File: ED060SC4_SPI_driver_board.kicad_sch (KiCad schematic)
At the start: 27 parts, among them J2 Conn_01x06, J3 Conn_01x04, J4 Conn_01x04, SW1 SS12D07VG2, SW2 DSIC01LSGET, U2 STM32F103C8T6, U3 USBLC6-4SC6, U4 USBLC6-2SC6, U5 USBLC6-2SC6, Y1 16MHz, 10pF

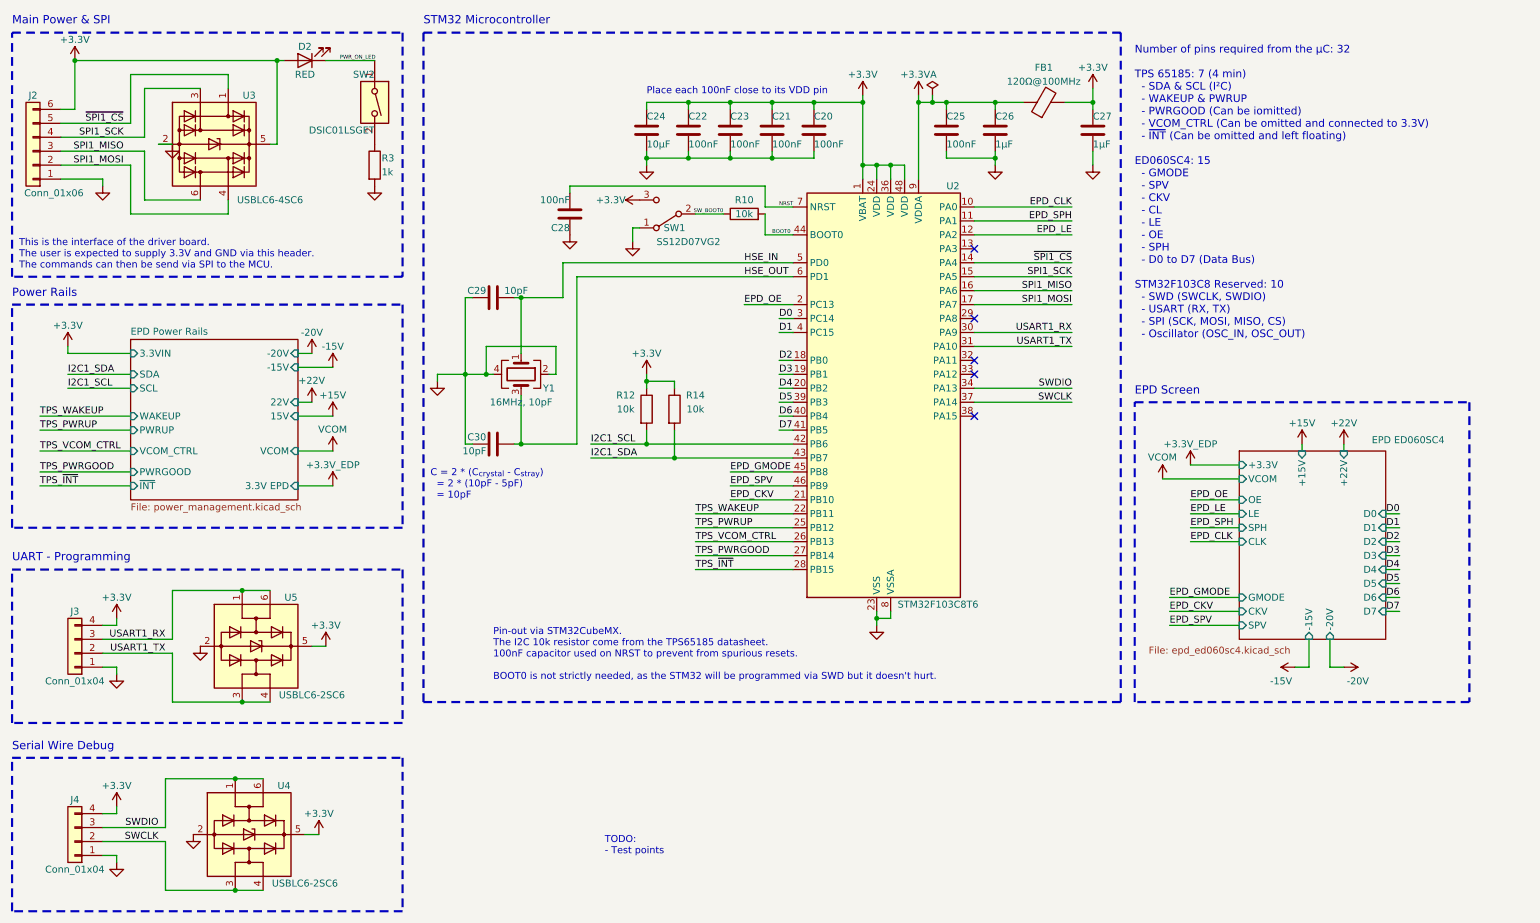
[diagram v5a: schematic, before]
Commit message: Fixed PWR flags in schematic
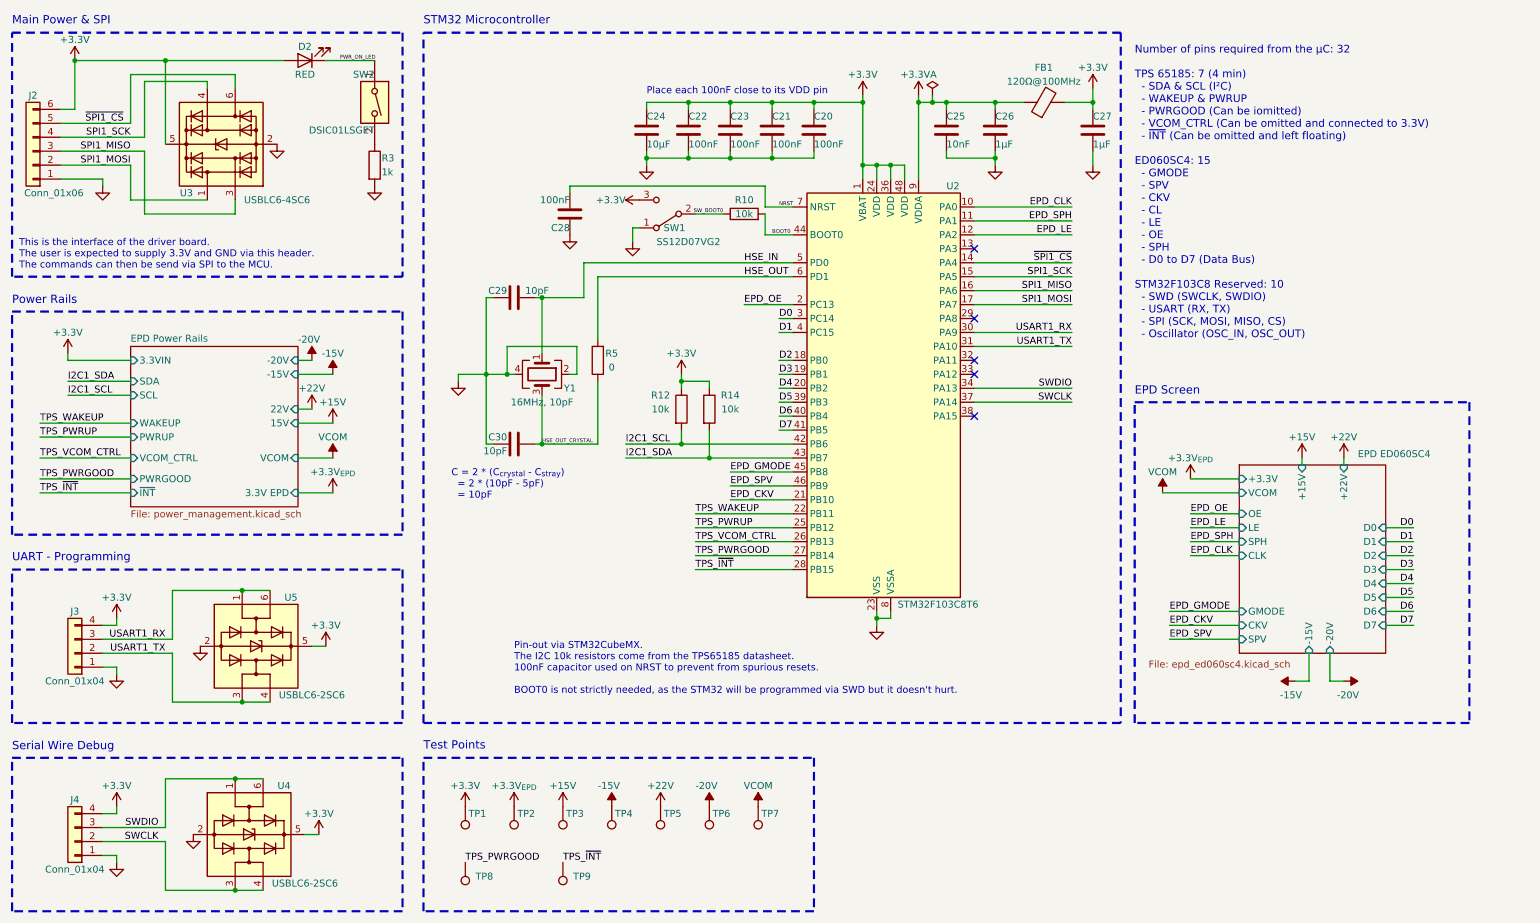
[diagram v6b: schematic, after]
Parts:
- added R5: 0, Resistor_SMD:R_0603_1608Metric, symbol Device:R
- added TP1, TP2, TP3, TP4, TP5, TP6, TP7, TP8, TP9: TestPoint, TestPoint:TestPoint_Pad_D1.0mm, symbol Connector:TestPoint
- C25: value 100nF -> 10nF
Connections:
- net +3.3V: now also TP1.1
- net HSE_OUT: now also R5.2; no longer C30.2, Y1.3
- net SPI1_MISO: now also U3.3 (I/O2); no longer U3.6 (I/O4)
- net SPI1_MOSI: now also U3.1 (I/O1); no longer U3.4 (I/O3)
- net SPI1_SCK: now also U3.4 (I/O3); no longer U3.3 (I/O2)
- net TPS_PWRGOOD: now also TP8.1
- net TPS_~{INT}: now also TP9.1
- net ~{SPI1_CS}: now also U3.6 (I/O4); no longer U3.1 (I/O1)
- new net +15V: TP3.1
- new net +22V: TP5.1
- new net +3.3V_{EPD}: TP2.1
- new net -15V: TP4.1
- new net -20V: TP6.1
- new net HSE_OUT_CRYSTAL: C30.2, R5.1, Y1.3
- new net VCOM: TP7.1
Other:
- note added: "Pin-out via STM32CubeMX. The I2C 10k resistors come from the TPS65185 datasheet. 100nF capacitor used on NRST to prevent from spurious resets. BOOT0 is not strictly needed, as the STM32 will be programmed via SWD but it doesn't hurt."
- note added: "Test Points"
- note removed: "Pin-out via STM32CubeMX. The I2C 10k resistor come from the TPS65185 datasheet. 100nF capacitor used on NRST to prevent from spurious resets. BOOT0 is not strictly needed, as the STM32 will be programmed via SWD but it doesn't hurt."
- note removed: "TODO: - Test points"
- moved on the sheet: C29, C30, R12, R14, U3, Y1

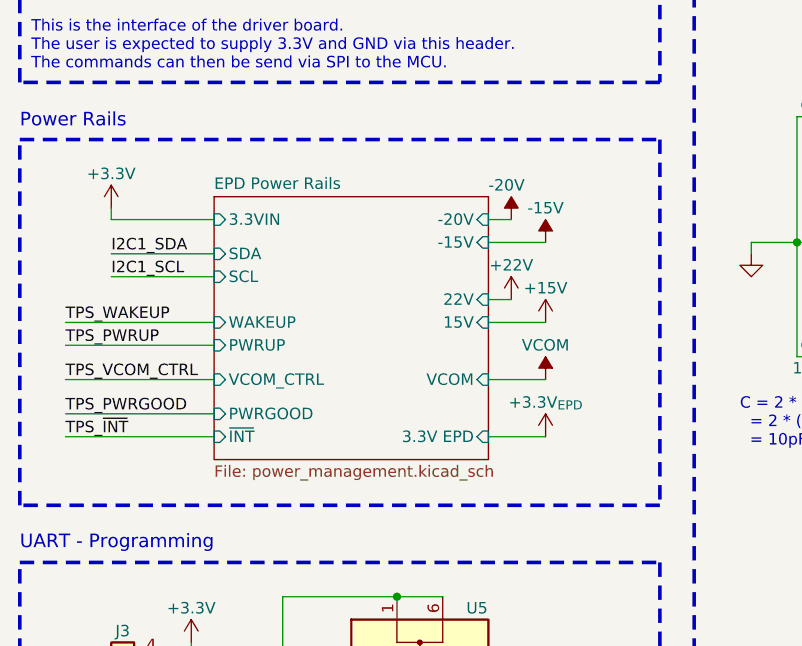
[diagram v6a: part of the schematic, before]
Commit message: Add a connector for easy access to voltages
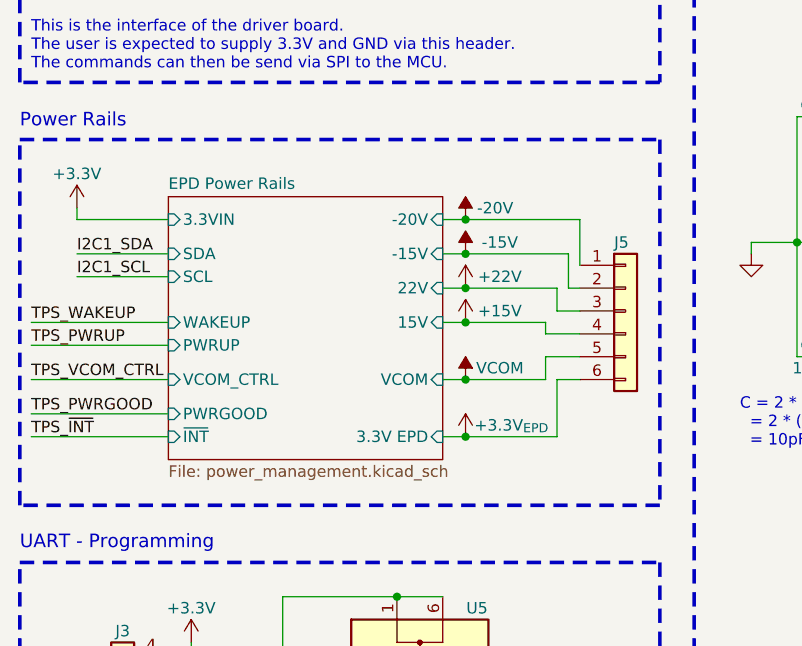
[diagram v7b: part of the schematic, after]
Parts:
- added J5: Conn_01x06, Connector_PinSocket_2.54mm:PinSocket_1x06_P2.54mm_Vertical, symbol Connector_Generic:Conn_01x06
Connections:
- net +15V: now also J5.4 (Pin_4)
- net +22V: now also J5.3 (Pin_3)
- net +3.3V_{EPD}: now also J5.6 (Pin_6)
- net -15V: now also J5.2 (Pin_2)
- net -20V: now also J5.1 (Pin_1)
- net VCOM: now also J5.5 (Pin_5)

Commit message: PCB routing
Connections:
- net SPI1_MISO: now also U3.1 (I/O1); no longer U3.3 (I/O2)
- net SPI1_MOSI: now also U3.3 (I/O2); no longer U3.1 (I/O1)
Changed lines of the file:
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@@
-    (stroke (width 0) (type default))
-  )
-  (wire (pts (xy 39.37 64.77) (xy 55.88 64.77))
     (stroke (width 0) (type default))
   )
@@
     (stroke (width 0) (type default))
   )
-  (wire (pts (xy 36.83 55.88) (xy 36.83 62.23))
+  (wire (pts (xy 36.83 55.88) (xy 36.83 64.77))
     (stroke (width 0) (type default))
   )
@@
     (stroke (width 0) (type default))
   )
-  (wire (pts (xy 36.83 62.23) (xy 50.8 62.23))
-    (stroke (width 0) (type default))
-  )
   (wire (pts (xy 212.09 41.91) (xy 212.09 44.45))
     (stroke (width 0) (type default))
@@
     (stroke (width 0) (type default))
   )
+  (wire (pts (xy 39.37 62.23) (xy 50.8 62.23))
+    (stroke (width 0) (type default))
+  )
   (wire (pts (xy 138.43 54.61) (xy 146.05 54.61))
     (stroke (width 0) (type default))
@@
     (stroke (width 0) (type default))
   )
-  (wire (pts (xy 39.37 53.34) (xy 39.37 64.77))
-    (stroke (width 0) (type default))
-  )
   (wire (pts (xy 139.7 121.92) (xy 157.48 121.92))
     (stroke (width 0) (type default))
@@
     (stroke (width 0) (type default))
   )
+  (wire (pts (xy 36.83 64.77) (xy 55.88 64.77))
+    (stroke (width 0) (type default))
+  )
   (wire (pts (xy 34.29 147.32) (xy 31.75 147.32))
     (stroke (width 0) (type default))
@@
     (stroke (width 0) (type default))
   )
+  (wire (pts (xy 39.37 53.34) (xy 39.37 62.23))
+    (stroke (width 0) (type default))
+  )
